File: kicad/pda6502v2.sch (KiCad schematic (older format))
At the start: 85 parts, among them J1 GPIO1, J2 GPIO2, J3 UART, J4 Screw_Terminal_01x02, J5 Conn_02x04_Odd_Even, J6 ICSP, J7 SPI, J8 FPGA_EXT, J9 SID, SW1 SW_Push, U1 W65C02SxP, U10 LT3030, U11 SC28L92A1B, U2 W65C22SxP, U3 W65C22SxP, U4 DS1818, U5 AS6C4008-55PCN, U6 ARMSID, U7 AT25M01, U8 ICE40HX4K-TQ144, U9 TLV1117-33, X1 8 MHz, X2 3.6864 MHz

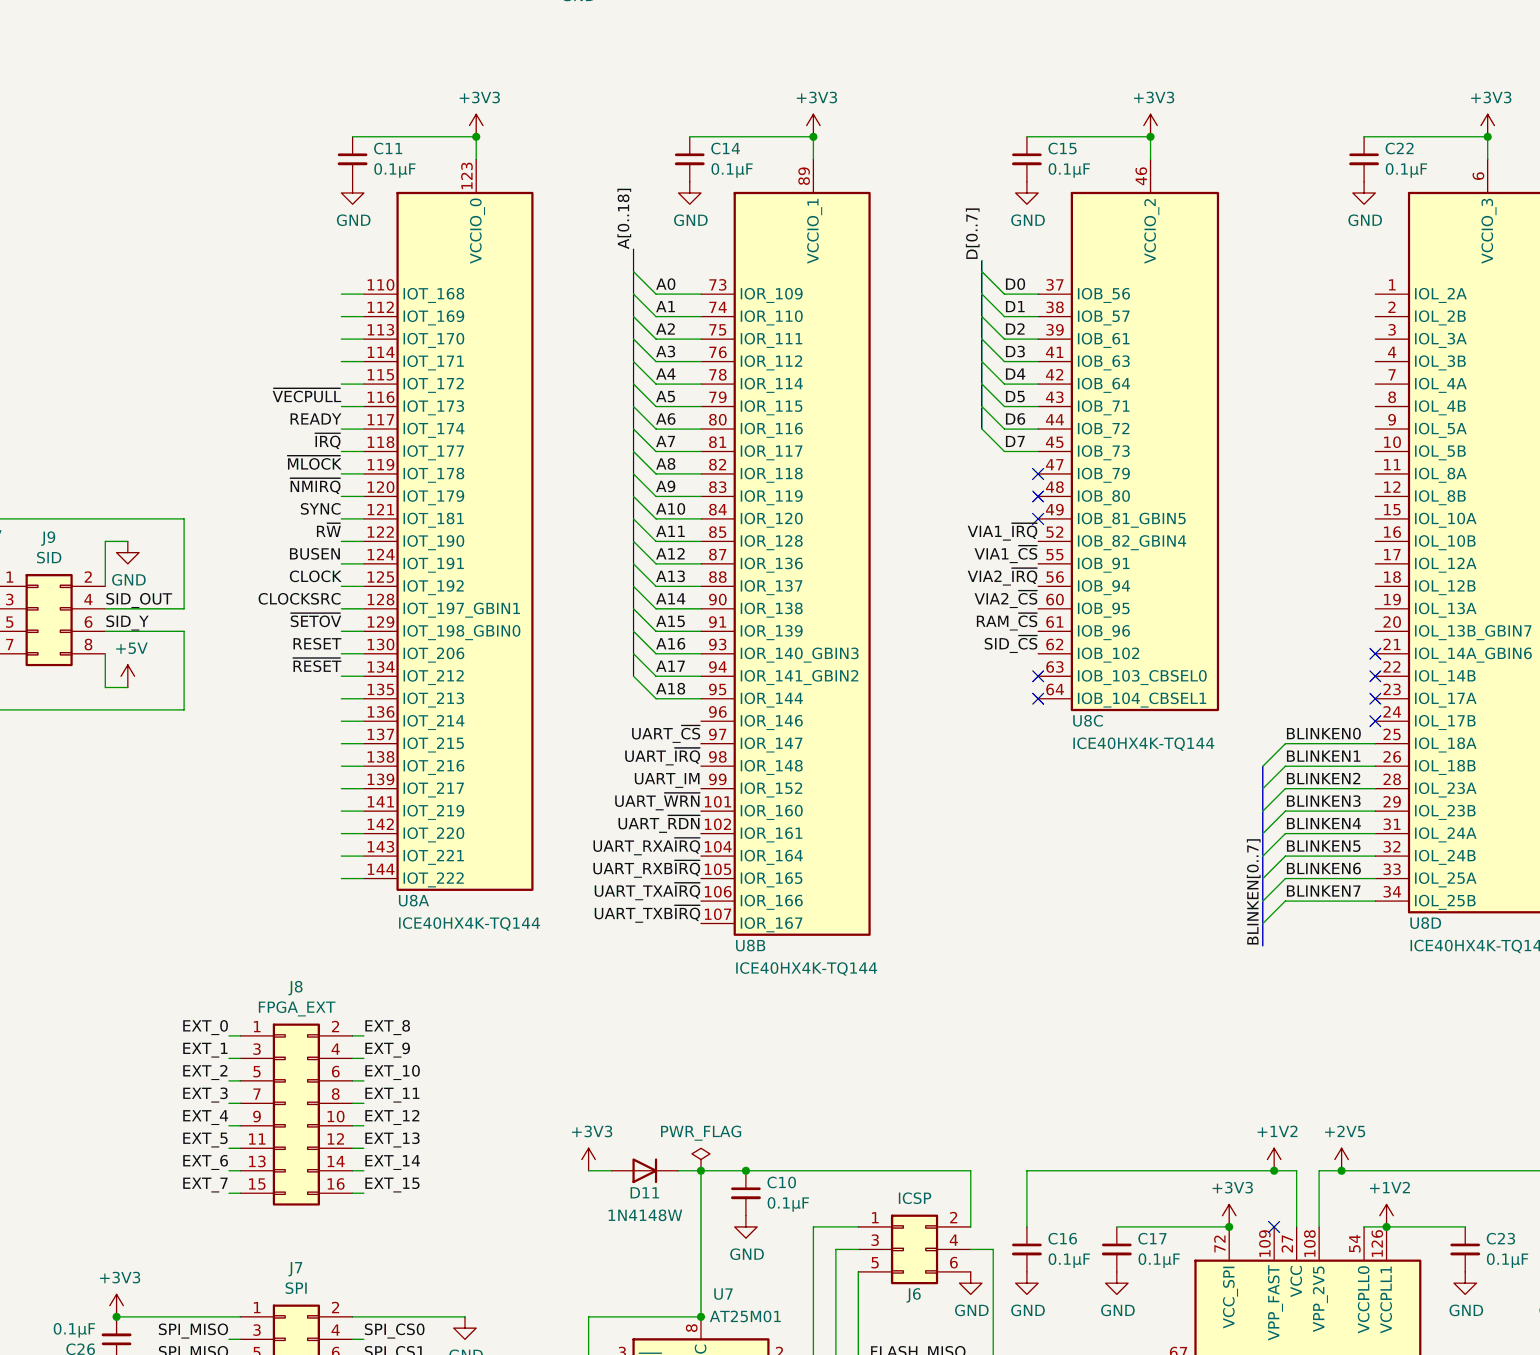
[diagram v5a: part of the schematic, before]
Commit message: Rearranged FPGA pin allocations for easier routing
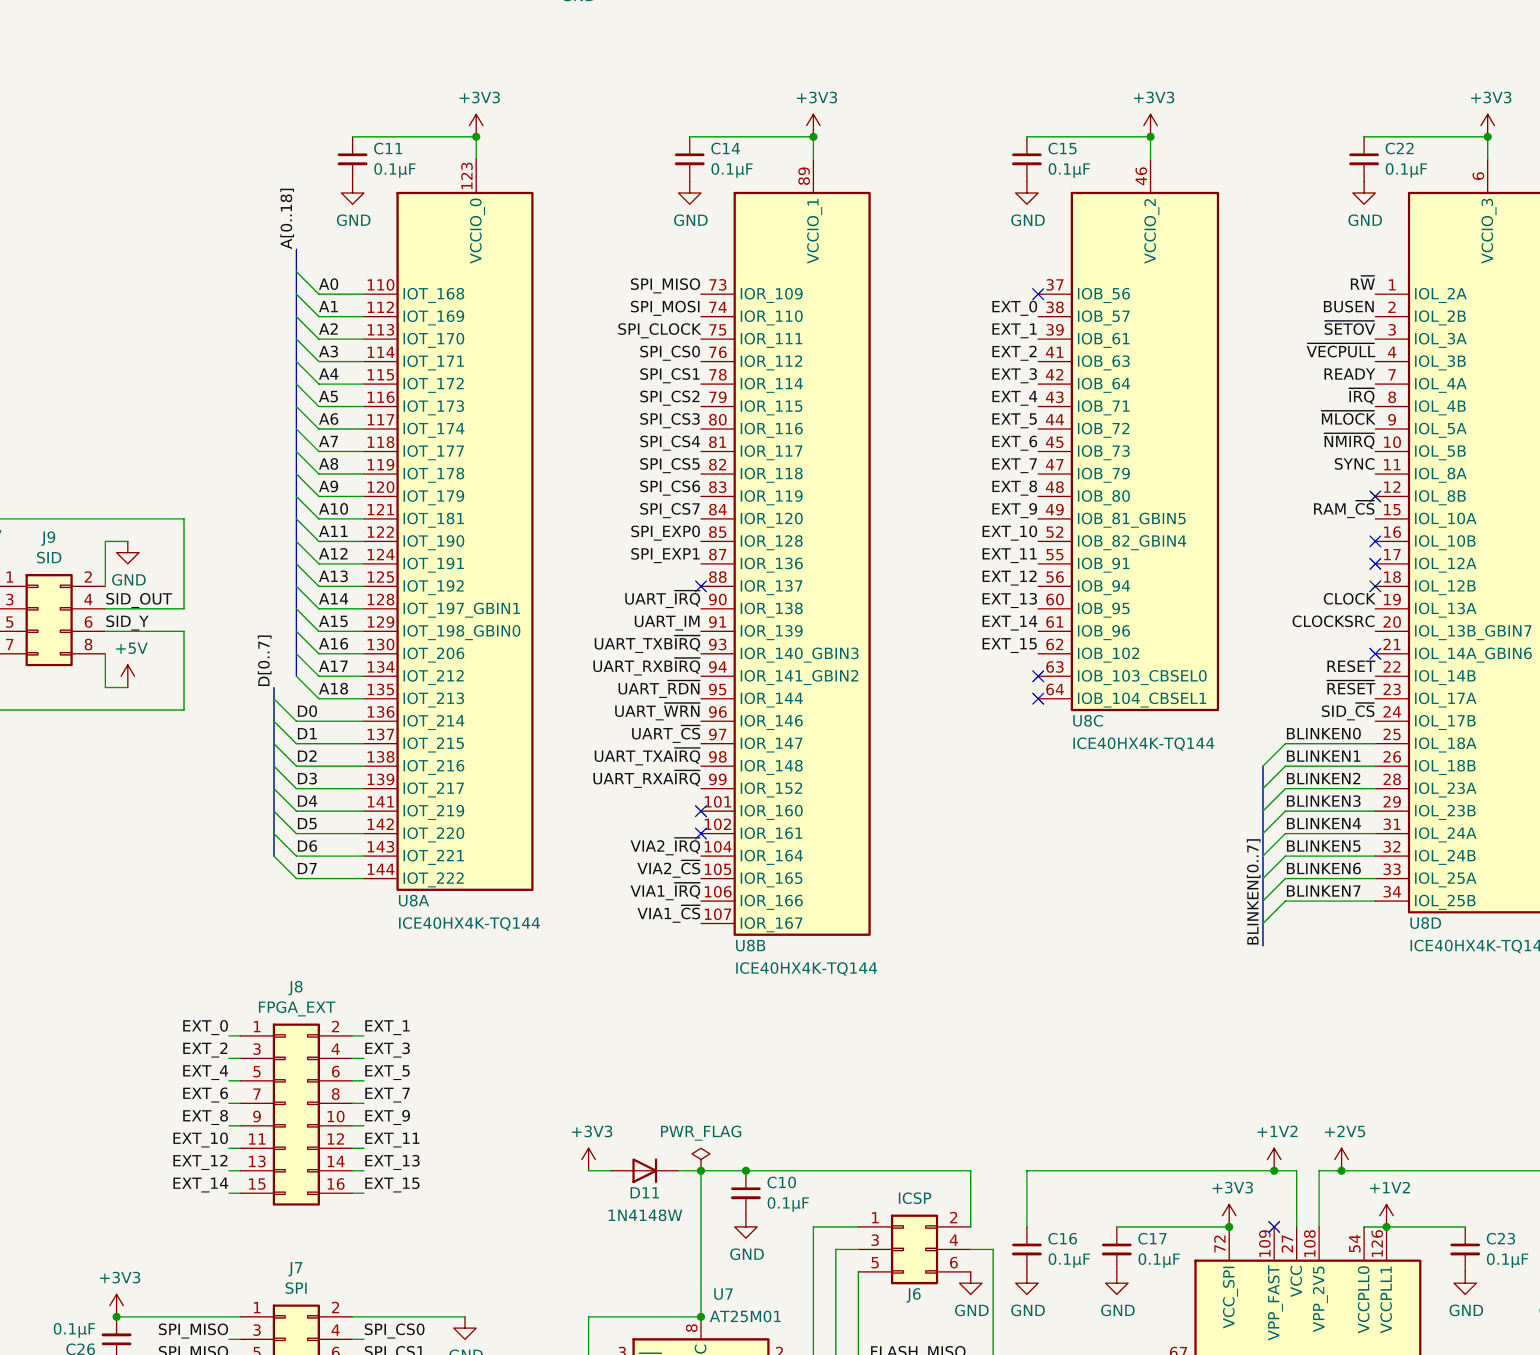
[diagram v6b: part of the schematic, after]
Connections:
- net A0: now also U8.110 (IOT_168); no longer U8.73 (IOR_109)
- net A1: now also U8.112 (IOT_169); no longer U8.74 (IOR_110)
- net A10: now also U8.121 (IOT_181); no longer U8.84 (IOR_120)
- net A11: now also U8.122 (IOT_190); no longer U8.85 (IOR_128)
- net A12: now also U8.124 (IOT_191); no longer U8.87 (IOR_136)
- net A13: now also U8.125 (IOT_192); no longer U8.88 (IOR_137)
- net A14: now also U8.128 (IOT_197_GBIN1); no longer U8.90 (IOR_138)
- net A15: now also U8.129 (IOT_198_GBIN0); no longer U8.91 (IOR_139)
- net A16: now also U8.130 (IOT_206); no longer U8.93 (IOR_140_GBIN3)
- net A17: now also U8.134 (IOT_212); no longer U8.94 (IOR_141_GBIN2)
- net A18: now also U8.135 (IOT_213); no longer U8.95 (IOR_144)
- net A2: now also U8.113 (IOT_170); no longer U8.75 (IOR_111)
- net A3: now also U8.114 (IOT_171); no longer U8.76 (IOR_112)
- net A4: now also U8.115 (IOT_172); no longer U8.78 (IOR_114)
- net A5: now also U8.116 (IOT_173); no longer U8.79 (IOR_115)
- net A6: now also U8.117 (IOT_174); no longer U8.80 (IOR_116)
- net A7: now also U8.118 (IOT_177); no longer U8.81 (IOR_117)
- net A8: now also U8.119 (IOT_178); no longer U8.82 (IOR_118)
- net A9: now also U8.120 (IOT_179); no longer U8.83 (IOR_119)
- net BUSEN: now also U8.2 (IOL_2B); no longer U8.124 (IOT_191)
- net CLOCK: now also U8.19 (IOL_13A); no longer U8.125 (IOT_192)
- net CLOCKSRC: now also U8.20 (IOL_13B_GBIN7); no longer U8.128 (IOT_197_GBIN1)
- net D0: now also U8.136 (IOT_214); no longer U8.37 (IOB_56)
- net D1: now also U8.137 (IOT_215); no longer U8.38 (IOB_57)
- net D2: now also U8.138 (IOT_216); no longer U8.39 (IOB_61)
- net D3: now also U8.139 (IOT_217); no longer U8.41 (IOB_63)
- net D4: now also U8.141 (IOT_219); no longer U8.42 (IOB_64)
- net D5: now also U8.142 (IOT_220); no longer U8.43 (IOB_71)
- net D6: now also U8.143 (IOT_221); no longer U8.44 (IOB_72)
- net D7: now also U8.144 (IOT_222); no longer U8.45 (IOB_73)
- net EXT_0: now also U8.38 (IOB_57)
- net EXT_1: now also J8.2 (Pin_2), U8.39 (IOB_61); no longer J8.3 (Pin_3)
- net EXT_10: now also J8.11 (Pin_11), U8.52 (IOB_82_GBIN4); no longer J8.6 (Pin_6)
- net EXT_11: now also J8.12 (Pin_12), U8.55 (IOB_91); no longer J8.8 (Pin_8)
- net EXT_12: now also J8.13 (Pin_13), U8.56 (IOB_94); no longer J8.10 (Pin_10)
- net EXT_13: now also J8.14 (Pin_14), U8.60 (IOB_95); no longer J8.12 (Pin_12)
- net EXT_14: now also J8.15 (Pin_15), U8.61 (IOB_96); no longer J8.14 (Pin_14)
- net EXT_15: now also U8.62 (IOB_102)
- net EXT_2: now also J8.3 (Pin_3), U8.41 (IOB_63); no longer J8.5 (Pin_5)
- net EXT_3: now also J8.4 (Pin_4), U8.42 (IOB_64); no longer J8.7 (Pin_7)
- net EXT_4: now also J8.5 (Pin_5), U8.43 (IOB_71); no longer J8.9 (Pin_9)
- net EXT_5: now also J8.6 (Pin_6), U8.44 (IOB_72); no longer J8.11 (Pin_11)
- net EXT_6: now also J8.7 (Pin_7), U8.45 (IOB_73); no longer J8.13 (Pin_13)
- net EXT_7: now also J8.8 (Pin_8), U8.47 (IOB_79); no longer J8.15 (Pin_15)
- net EXT_8: now also J8.9 (Pin_9), U8.48 (IOB_80); no longer J8.2 (Pin_2)
- net EXT_9: now also J8.10 (Pin_10), U8.49 (IOB_81_GBIN5); no longer J8.4 (Pin_4)
- net RAM_~CS: now also U8.15 (IOL_10A); no longer U8.61 (IOB_96)
- net READY: now also U8.7 (IOL_4A); no longer U8.117 (IOT_174)
- net RESET: now also U8.22 (IOL_14B); no longer U8.130 (IOT_206)
- net R~W: now also U8.1 (IOL_2A); no longer U8.122 (IOT_190)
- net SID_~CS: now also U8.24 (IOL_17B); no longer U8.62 (IOB_102)
- net SPI_CLOCK: now also U8.75 (IOR_111)
- net SPI_CS0: now also U8.76 (IOR_112)
- net SPI_CS1: now also U8.78 (IOR_114)
- net SPI_CS2: now also U8.79 (IOR_115)
- net SPI_CS3: now also U8.80 (IOR_116)
- net SPI_CS4: now also U8.81 (IOR_117)
- net SPI_CS5: now also U8.82 (IOR_118)
- net SPI_CS6: now also U8.83 (IOR_119)
- net SPI_CS7: now also U8.84 (IOR_120)
- net SPI_EXP0: now also U8.85 (IOR_128)
- net SPI_EXP1: now also U8.87 (IOR_136)
- net SPI_MISO: now also U8.73 (IOR_109)
- net SPI_MOSI: now also U8.74 (IOR_110)
- net SYNC: now also U8.11 (IOL_8A); no longer U8.121 (IOT_181)
- net UART_IM: now also U8.91 (IOR_139); no longer U8.99 (IOR_152)
- net UART_RXA~IRQ: now also U8.99 (IOR_152); no longer U8.104 (IOR_164)
- net UART_RXB~IRQ: now also U8.94 (IOR_141_GBIN2); no longer U8.105 (IOR_165)
- net UART_TXA~IRQ: now also U8.98 (IOR_148); no longer U8.106 (IOR_166)
- net UART_TXB~IRQ: now also U8.93 (IOR_140_GBIN3); no longer U8.107 (IOR_167)
- net UART_~IRQ: now also U8.90 (IOR_138); no longer U8.98 (IOR_148)
- net UART_~RDN: now also U8.95 (IOR_144); no longer U8.102 (IOR_161)
- net UART_~WRN: now also U8.96 (IOR_146); no longer U8.101 (IOR_160)
- net VIA1_~CS: now also U8.107 (IOR_167); no longer U8.55 (IOB_91)
- net VIA1_~IRQ: now also U8.106 (IOR_166); no longer U8.52 (IOB_82_GBIN4)
- net VIA2_~CS: now also U8.105 (IOR_165); no longer U8.60 (IOB_95)
- net VIA2_~IRQ: now also U8.104 (IOR_164); no longer U8.56 (IOB_94)
- net ~IRQ: now also U8.8 (IOL_4B); no longer U8.118 (IOT_177)
- net ~MLOCK: now also U8.9 (IOL_5A); no longer U8.119 (IOT_178)
- net ~NMIRQ: now also U8.10 (IOL_5B); no longer U8.120 (IOT_179)
- net ~RESET: now also U8.23 (IOL_17A); no longer U8.134 (IOT_212)
- net ~SETOV: now also U8.3 (IOL_3A); no longer U8.129 (IOT_198_GBIN0)
- net ~VECPULL: now also U8.4 (IOL_3B); no longer U8.116 (IOT_173)
- no-connect marks 25 -> 27

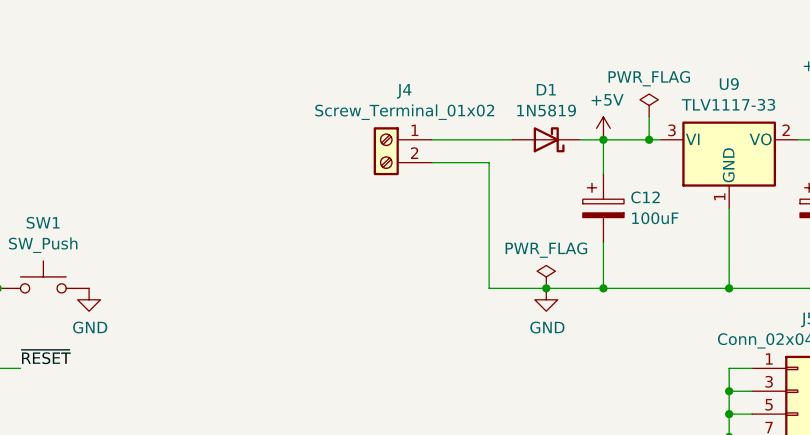
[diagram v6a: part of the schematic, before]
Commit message: Routing begins; FPGA to EXT & SPI headers.
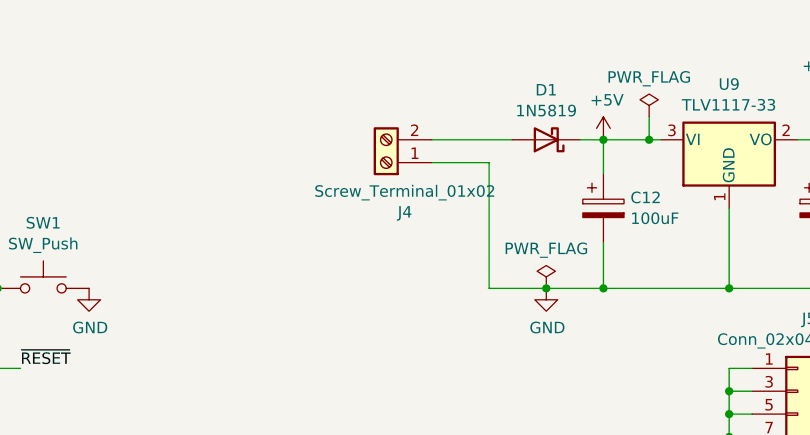
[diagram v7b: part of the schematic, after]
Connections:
- net GND: now also J4.1 (Pin_1); no longer J4.2 (Pin_2)
- net at D1.2 (A): now also J4.2 (Pin_2); no longer J4.1 (Pin_1)
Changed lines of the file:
@@
 L Connector:Screw_Terminal_01x02 J4
 U 1 1 628F567C
-P 9700 1100
-F 0 "J4" H 9618 1317 50  0000 C CNN
-F 1 "Screw_Terminal_01x02" H 9618 1226 50  0000 C CNN
-F 2 "TerminalBlock_Phoenix:TerminalBlock_Phoenix_MPT-0,5-2-2.54_1x02_P2.54mm_Horizontal" H 9700 1100 50  0001 C CNN
-F 3 "~" H 9700 1100 50  0001 C CNN
-	1    9700 1100
-	-1   0    0    -1
+P 9700 1200
+F 0 "J4" H 9618 1417 50  0000 C CNN
+F 1 "Screw_Terminal_01x02" H 9618 1326 50  0000 C CNN
+F 2 "TerminalBlock_Phoenix:TerminalBlock_Phoenix_MPT-0,5-2-2.54_1x02_P2.54mm_Horizontal" H 9700 1200 50  0001 C CNN
+F 3 "~" H 9700 1200 50  0001 C CNN
+	1    9700 1200
+	-1   0    0    1
 $EndComp
 Connection ~ 10400 1750

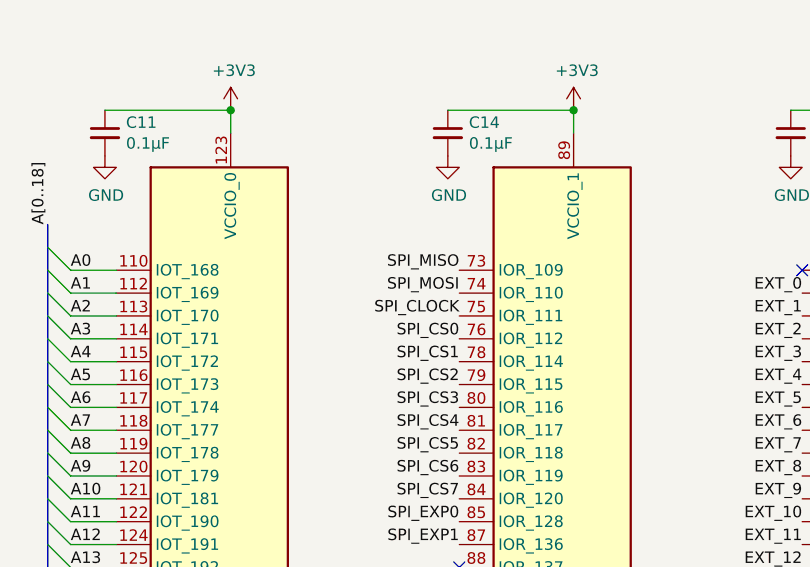
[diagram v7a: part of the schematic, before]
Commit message: FPGA EXT/SPI routing tweaks, UART moved down/right
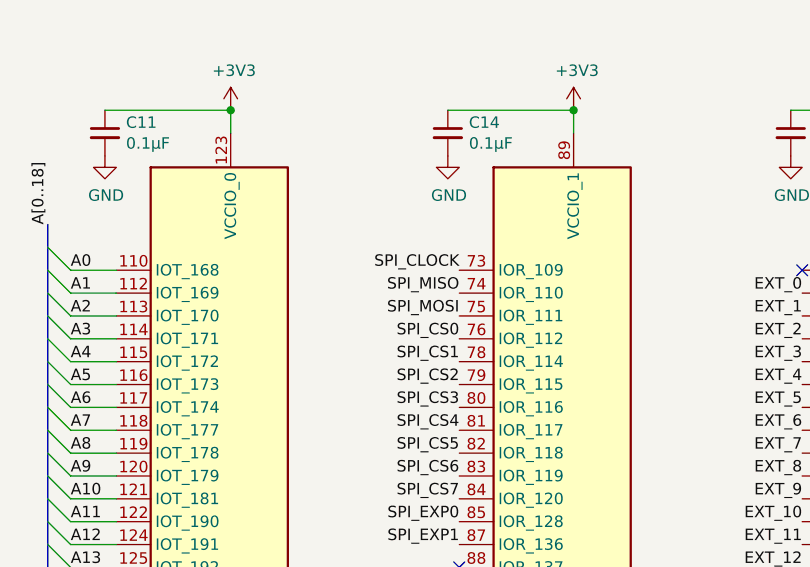
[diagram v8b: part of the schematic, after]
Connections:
- net SPI_CLOCK: now also U8.73 (IOR_109); no longer U8.75 (IOR_111)
- net SPI_MISO: now also U8.74 (IOR_110); no longer U8.73 (IOR_109)
- net SPI_MOSI: now also U8.75 (IOR_111); no longer U8.74 (IOR_110)
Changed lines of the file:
@@
 Wire Wire Line
 	9950 6550 10250 6550
+Text Label 11750 4050 2    50   ~ 0
+SPI_MISO
+Text Label 11750 4150 2    50   ~ 0
+SPI_MOSI
 Text Label 11750 3950 2    50   ~ 0
-SPI_MISO
-Text Label 11750 4050 2    50   ~ 0
-SPI_MOSI
-Text Label 11750 4150 2    50   ~ 0
 SPI_CLOCK
 Text Label 11750 4250 2    50   ~ 0
